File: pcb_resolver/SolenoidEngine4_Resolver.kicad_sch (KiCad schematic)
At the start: 2 parts, among them J15 Screw_Terminal_01x03, J16 Screw_Terminal_01x03

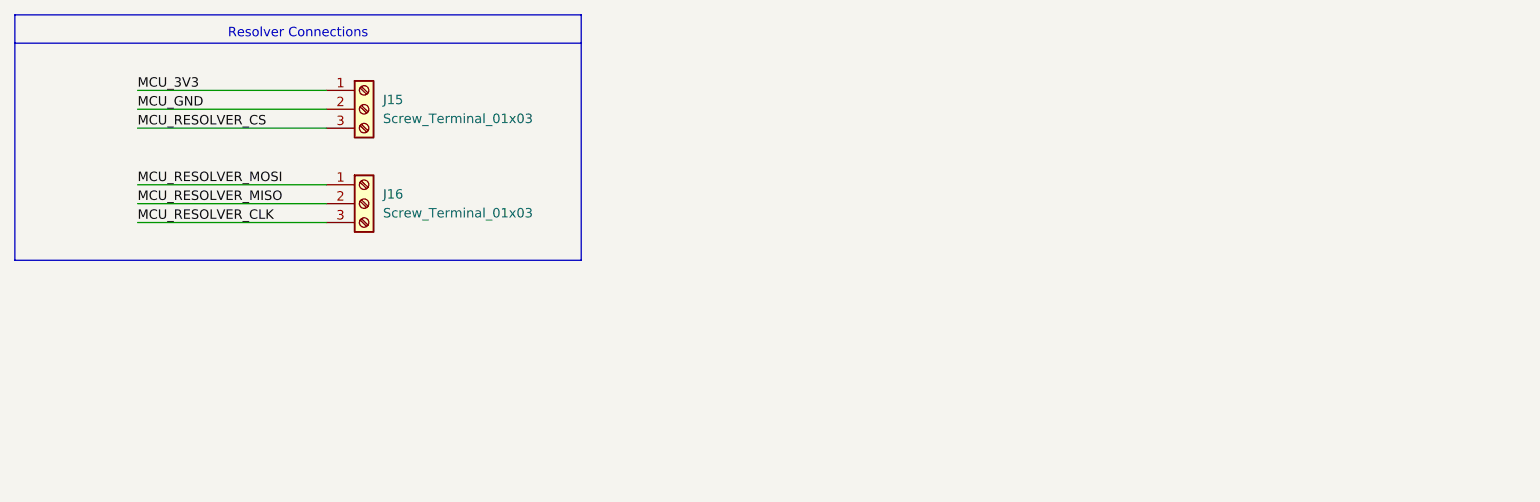
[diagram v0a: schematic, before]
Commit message: Resolver PCB nearly done
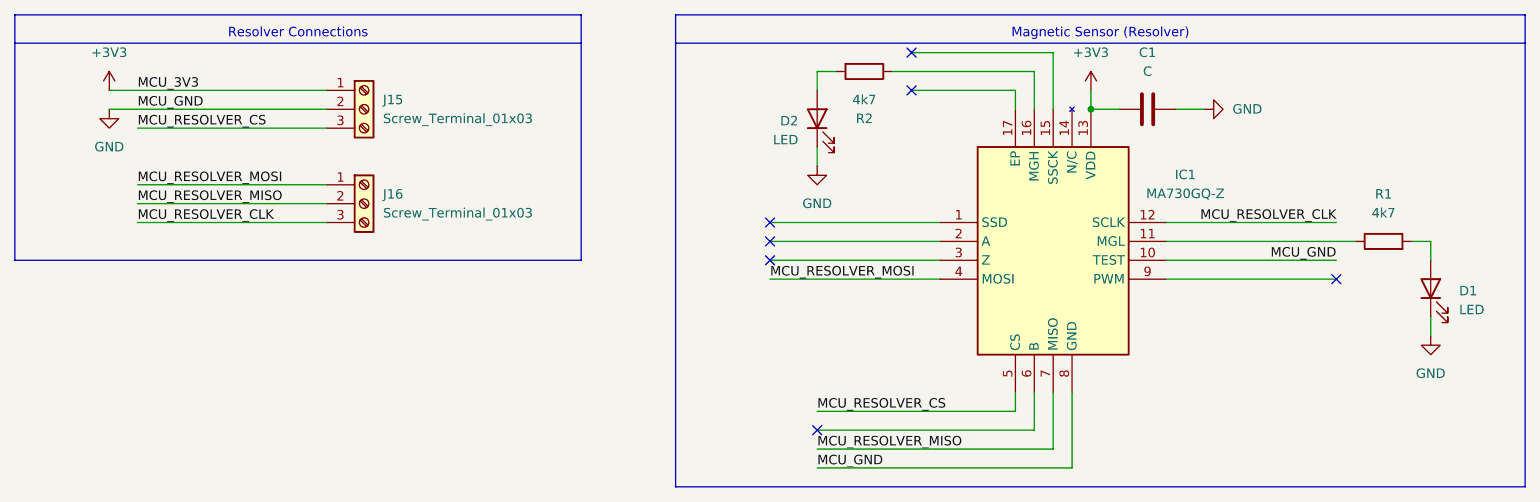
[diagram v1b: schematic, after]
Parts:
- added C1: C, symbol Device:C
- added D1, D2: LED, symbol Device:LED
- added IC1: MA730GQ-Z, footprints:QFN50P300X300X100-17N-D, symbol MA730GQ-Z:MA730GQ-Z
- added R1, R2: 4k7, symbol Device:R
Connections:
- net MCU_RESOLVER_CLK: now also IC1.12 (SCLK)
- net MCU_RESOLVER_CS: now also IC1.5 (CS)
- net MCU_RESOLVER_MISO: now also IC1.7 (MISO)
- net MCU_RESOLVER_MOSI: now also IC1.4 (MOSI)
- net MCU_3V3 renamed +3V3
- net +3V3: now also C1.1, IC1.13 (VDD)
- net MCU_GND renamed GND
- net GND: now also C1.2, D1.1 (K), D2.1 (K), IC1.10 (TEST), IC1.8 (GND)
- new net: IC1.16 (MGH), R2.1
- new net: D2.2 (A), R2.2
- new net: IC1.11 (MGL), R1.1
- new net: D1.2 (A), R1.2
- no-connect marks 0 -> 7
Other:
- note added: "Magnetic Sensor (Resolver)"
